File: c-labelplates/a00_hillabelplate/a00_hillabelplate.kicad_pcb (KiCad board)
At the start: 2 copper layers, 43 x 8 mm, 2 parts

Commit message: single gerbers
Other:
- board text added: "A00_hillabelplate"
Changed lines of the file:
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@@
       (outputformat 1)
       (mirror false)
-      (drillshape 1)
+      (drillshape 0)
       (scaleselection 1)
-      (outputdirectory "")
+      (outputdirectory "gerber/single/")
     )
   )
@@
   )
   (gr_circle (center 124.7 104) (end 124.78 104) (layer "F.SilkS") (width 0.15) (fill none))
+  (gr_line (start 110.4 100) (end 110.4 100.25) (layer "F.SilkS") (width 0.5))
   (gr_circle (center 130.75 101.3) (end 130.83 101.3) (layer "F.SilkS") (width 0.15) (fill none))
   (gr_circle (center 132.1 101.3) (end 132.18 101.3) (layer "F.SilkS") (width 0.15) (fill none))
   (gr_circle (center 128.4 104) (end 128.48 104) (layer "F.SilkS") (width 0.15) (fill none))
+  (gr_line (start 121.5 107.75) (end 121.5 108) (layer "F.SilkS") (width 0.5))
   (gr_circle (center 121 104) (end 121.08 104) (layer "F.SilkS") (width 0.15) (fill none))
   (gr_circle (center 125.7 101.3) (end 125.78 101.3) (layer "F.SilkS") (width 0.15) (fill none))
@@
   (gr_circle (center 113.6 106.7) (end 113.68 106.7) (layer "F.SilkS") (width 0.15) (fill none))
   (gr_circle (center 114.6 106.7) (end 114.68 106.7) (layer "F.SilkS") (width 0.15) (fill none))
+  (gr_line (start 125.2 107.75) (end 125.2 108) (layer "F.SilkS") (width 0.5))
+  (gr_line (start 128.9 100) (end 128.9 100.25) (layer "F.SilkS") (width 0.5))
   (gr_circle (center 118.3 104) (end 118.38 104) (layer "F.SilkS") (width 0.15) (fill none))
   (gr_circle (center 129.4 106.7) (end 129.48 106.7) (layer "F.SilkS") (width 0.15) (fill none))
@@
   (gr_circle (center 139.5 104) (end 139.58 104) (layer "F.SilkS") (width 0.15) (fill none))
   (gr_circle (center 132.1 104) (end 132.18 104) (layer "F.SilkS") (width 0.15) (fill none))
+  (gr_line (start 136.3 107.75) (end 136.3 108) (layer "F.SilkS") (width 0.5))
   (gr_circle (center 138.15 104) (end 138.23 104) (layer "F.SilkS") (width 0.15) (fill none))
   (gr_circle (center 132.1 106.7) (end 132.18 106.7) (layer "F.SilkS") (width 0.15) (fill none))
   (gr_circle (center 103.5 101.3) (end 103.58 101.3) (layer "F.SilkS") (width 0.15) (fill none))
+  (gr_line (start 117.8 100) (end 117.8 100.25) (layer "F.SilkS") (width 0.5))
   (gr_circle (center 134.45 106.7) (end 134.53 106.7) (layer "F.SilkS") (width 0.15) (fill none))
   (gr_circle (center 133.1 106.7) (end 133.18 106.7) (layer "F.SilkS") (width 0.15) (fill none))
@@
   (gr_circle (center 113.6 104) (end 113.68 104) (layer "F.SilkS") (width 0.15) (fill none))
   (gr_circle (center 136.8 106.7) (end 136.88 106.7) (layer "F.SilkS") (width 0.15) (fill none))
+  (gr_line (start 136.3 100) (end 136.3 100.25) (layer "F.SilkS") (width 0.5))
   (gr_circle (center 103.5 104) (end 103.58 104) (layer "F.SilkS") (width 0.15) (fill none))
   (gr_circle (center 119.65 106.7) (end 119.73 106.7) (layer "F.SilkS") (width 0.15) (fill none))
   (gr_circle (center 136.8 104) (end 136.88 104) (layer "F.SilkS") (width 0.15) (fill none))
   (gr_circle (center 136.8 101.3) (end 136.88 101.3) (layer "F.SilkS") (width 0.15) (fill none))
+  (gr_line (start 106.7 107.75) (end 106.7 108) (layer "F.SilkS") (width 0.5))
   (gr_circle (center 129.4 101.3) (end 129.48 101.3) (layer "F.SilkS") (width 0.15) (fill none))
   (gr_circle (center 124.7 101.3) (end 124.78 101.3) (layer "F.SilkS") (width 0.15) (fill none))
+  (gr_line (start 117.8 107.75) (end 117.8 108) (layer "F.SilkS") (width 0.5))
   (gr_circle (center 133.1 101.3) (end 133.18 101.3) (layer "F.SilkS") (width 0.15) (fill none))
   (gr_circle (center 134.45 101.3) (end 134.53 101.3) (layer "F.SilkS") (width 0.15) (fill none))
   (gr_circle (center 115.95 106.7) (end 116.03 106.7) (layer "F.SilkS") (width 0.15) (fill none))
+  (gr_line (start 132.6 100) (end 132.6 100.25) (layer "F.SilkS") (width 0.5))
   (gr_circle (center 106.2 104) (end 106.28 104) (layer "F.SilkS") (width 0.15) (fill none))
   (gr_circle (center 122 106.7) (end 122.08 106.7) (layer "F.SilkS") (width 0.15) (fill none))
@@
   (gr_circle (center 134.45 104) (end 134.53 104) (layer "F.SilkS") (width 0.15) (fill none))
   (gr_circle (center 124.7 106.7) (end 124.78 106.7) (layer "F.SilkS") (width 0.15) (fill none))
+  (gr_line (start 121.5 100) (end 121.5 100.25) (layer "F.SilkS") (width 0.5))
   (gr_circle (center 109.9 101.3) (end 109.98 101.3) (layer "F.SilkS") (width 0.15) (fill none))
   (gr_circle (center 122 104) (end 122.08 104) (layer "F.SilkS") (width 0.15) (fill none))
@@
   (gr_circle (center 138.15 101.3) (end 138.23 101.3) (layer "F.SilkS") (width 0.15) (fill none))
   (gr_circle (center 103.5 106.7) (end 103.58 106.7) (layer "F.SilkS") (width 0.15) (fill none))
+  (gr_line (start 128.9 107.75) (end 128.9 108) (layer "F.SilkS") (width 0.5))
   (gr_circle (center 123.35 106.7) (end 123.43 106.7) (layer "F.SilkS") (width 0.15) (fill none))
   (gr_circle (center 127.05 106.7) (end 127.13 106.7) (layer "F.SilkS") (width 0.15) (fill none))
   (gr_circle (center 114.6 101.3) (end 114.68 101.3) (layer "F.SilkS") (width 0.15) (fill none))
   (gr_line (start 100 100) (end 143 100) (layer "F.SilkS") (width 0.5))
+  (gr_line (start 125.2 100) (end 125.2 100.25) (layer "F.SilkS") (width 0.5))
   (gr_circle (center 104.85 104) (end 104.93 104) (layer "F.SilkS") (width 0.15) (fill none))
   (gr_line (start 100 108) (end 143 108) (layer "F.SilkS") (width 0.5))
@@
   (gr_circle (center 107.2 106.7) (end 107.28 106.7) (layer "F.SilkS") (width 0.15) (fill none))
   (gr_circle (center 112.25 106.7) (end 112.33 106.7) (layer "F.SilkS") (width 0.15) (fill none))
+  (gr_line (start 110.4 107.75) (end 110.4 108) (layer "F.SilkS") (width 0.5))
   (gr_circle (center 109.9 106.7) (end 109.98 106.7) (layer "F.SilkS") (width 0.15) (fill none))
   (gr_circle (center 113.6 101.3) (end 113.68 101.3) (layer "F.SilkS") (width 0.15) (fill none))
@@
   (gr_circle (center 127.05 104) (end 127.13 104) (layer "F.SilkS") (width 0.15) (fill none))
   (gr_circle (center 110.9 101.3) (end 110.98 101.3) (layer "F.SilkS") (width 0.15) (fill none))
+  (gr_line (start 114.1 100) (end 114.1 100.25) (layer "F.SilkS") (width 0.5))
   (gr_circle (center 117.3 104) (end 117.38 104) (layer "F.SilkS") (width 0.15) (fill none))
   (gr_circle (center 127.05 101.3) (end 127.13 101.3) (layer "F.SilkS") (width 0.15) (fill none))
   (gr_circle (center 139.5 101.3) (end 139.58 101.3) (layer "F.SilkS") (width 0.15) (fill none))
+  (gr_line (start 106.7 100) (end 106.7 100.25) (layer "F.SilkS") (width 0.5))
+  (gr_line (start 114.1 107.75) (end 114.1 108) (layer "F.SilkS") (width 0.5))
   (gr_circle (center 135.8 106.7) (end 135.88 106.7) (layer "F.SilkS") (width 0.15) (fill none))
   (gr_circle (center 115.95 101.3) (end 116.03 101.3) (layer "F.SilkS") (width 0.15) (fill none))
@@
   (gr_circle (center 135.8 101.3) (end 135.88 101.3) (layer "F.SilkS") (width 0.15) (fill none))
   (gr_circle (center 107.2 101.3) (end 107.28 101.3) (layer "F.SilkS") (width 0.15) (fill none))
+  (gr_line (start 132.6 107.75) (end 132.6 108) (layer "F.SilkS") (width 0.5))
   (gr_circle (center 119.65 104) (end 119.73 104) (layer "F.SilkS") (width 0.15) (fill none))
   (gr_line (start 136.3 100) (end 136.3 108) (layer "Cmts.User") (width 0.15))
@@
   (gr_line (start 100 108) (end 143 108) (layer "Edge.Cuts") (width 0.1))
   (gr_line (start 143 100) (end 143 108) (layer "Edge.Cuts") (width 0.1))
+  (gr_text "A00_hillabelplate" (at 133.35 106.299) (layer "B.SilkS")
+    (effects (font (size 1 1) (thickness 0.15)) (justify mirror))
+  )
 )

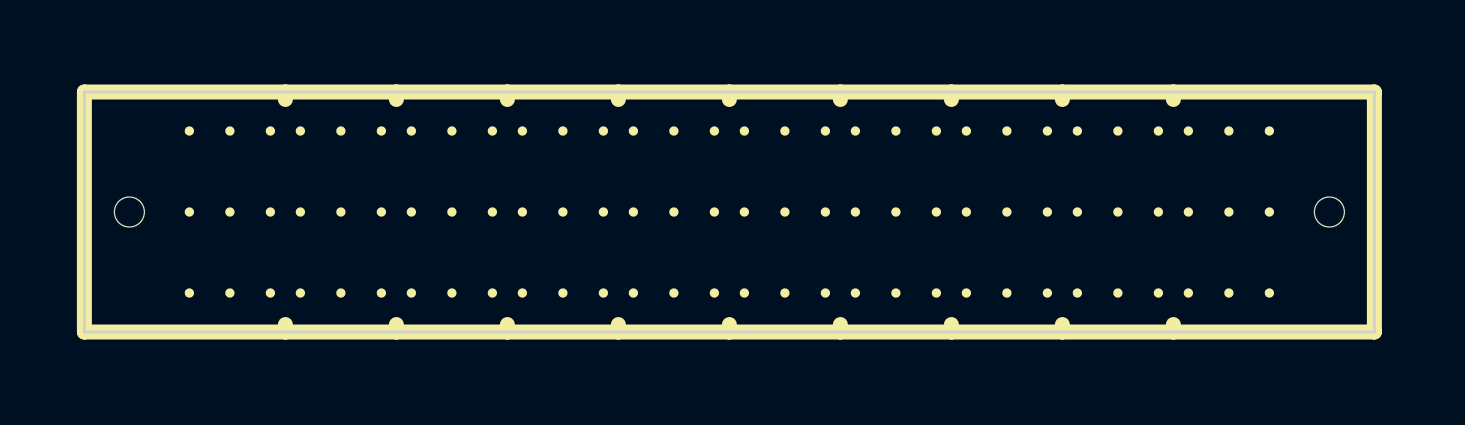
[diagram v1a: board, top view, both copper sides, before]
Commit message: added copper planes
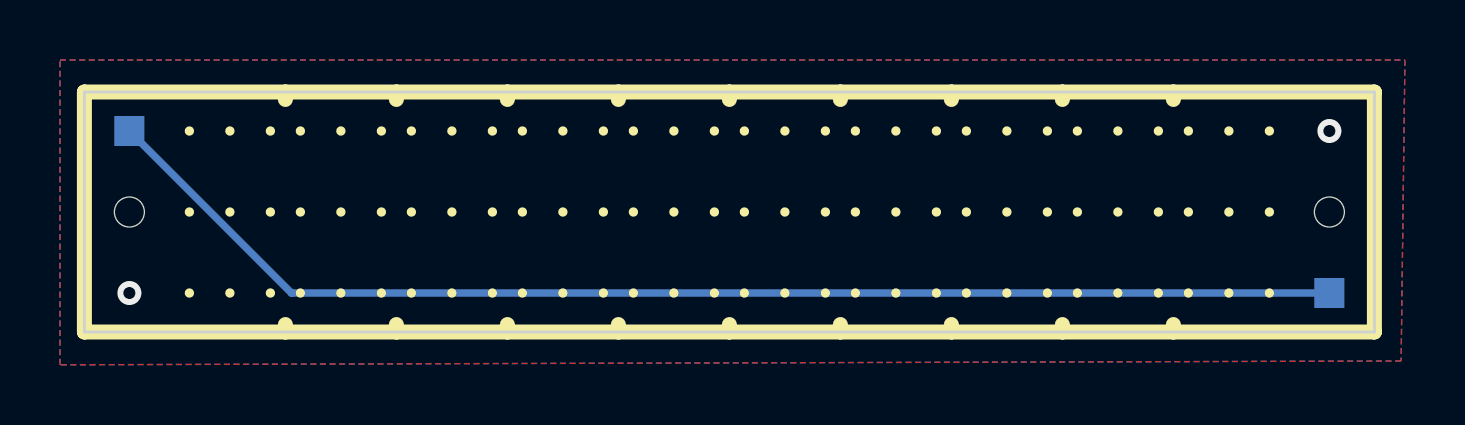
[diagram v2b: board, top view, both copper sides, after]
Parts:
- added TP1: TestPoint, TestPoint:TestPoint_Pad_1.0x1.0mm, B.Cu at (101.5, 101.3)
- added TP2: TestPoint, TestPoint:TestPoint_Pad_1.0x1.0mm, B.Cu at (141.5, 106.7)
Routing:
- net GND: track 0.00 -> 42.2 mm, vias 0 -> 2
- added copper zone on B.Cu, net GND
- added copper zone on F.Cu, net GND
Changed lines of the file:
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@@
   )
   (net 0 "")
+  (net 1 "GND")
   (footprint "MountingHoleSmall:MountingHole_1mm" (layer "F.Cu")
     (at 101.5 104)
@@
     (fp_circle (center 0 0) (end 1.25 0) (layer "F.CrtYd") (width 0.05) (fill none))
     (pad "" np_thru_hole circle locked (at 0 0) (size 1 1) (drill 1) (layers *.Cu *.Mask))
+  )
+  (footprint "TestPoint:TestPoint_Pad_1.0x1.0mm" (layer "B.Cu")
+    (at 141.5 106.7 180)
+    (descr "SMD rectangular pad as test Point, square 1.0mm side length")
+    (tags "test point SMD pad rectangle square")
+    (property "Sheetfile" "a00_hillabelplate.kicad_sch")
+    (property "Sheetname" "")
+    (attr exclude_from_pos_files)
+    (fp_text reference "TP2" (at 0 1.448) (layer "B.SilkS") hide
+      (effects (font (size 1 1) (thickness 0.15)) (justify mirror))
+    )
+    (fp_text value "TestPoint" (at 0 -1.55) (layer "B.Fab")
+      (effects (font (size 1 1) (thickness 0.15)) (justify mirror))
+    )
+    (fp_text user "${REFERENCE}" (at 0 1.45) (layer "B.Fab")
+      (effects (font (size 1 1) (thickness 0.15)) (justify mirror))
+    )
+    (fp_line (start -0.7 -0.7) (end -0.7 0.7) (layer "B.SilkS") (width 0.12))
+    (fp_line (start 0.7 0.7) (end 0.7 -0.7) (layer "B.SilkS") (width 0.12))
+    (fp_line (start 0.7 -0.7) (end -0.7 -0.7) (layer "B.SilkS") (width 0.12))
+    (fp_line (start -0.7 0.7) (end 0.7 0.7) (layer "B.SilkS") (width 0.12))
+    (fp_line (start -1 1) (end -1 -1) (layer "B.CrtYd") (width 0.05))
+    (fp_line (start -1 1) (end 1 1) (layer "B.CrtYd") (width 0.05))
+    (fp_line (start 1 -1) (end 1 1) (layer "B.CrtYd") (width 0.05))
+    (fp_line (start 1 -1) (end -1 -1) (layer "B.CrtYd") (width 0.05))
+    (pad "1" smd rect (at 0 0 180) (size 1 1) (layers "B.Cu" "B.Mask")
+      (net 1 "GND") (pinfunction "1") (pintype "passive"))
+  )
+  (footprint "TestPoint:TestPoint_Pad_1.0x1.0mm" (layer "B.Cu")
+    (at 101.5 101.3 180)
+    (descr "SMD rectangular pad as test Point, square 1.0mm side length")
+    (tags "test point SMD pad rectangle square")
+    (property "Sheetfile" "a00_hillabelplate.kicad_sch")
+    (property "Sheetname" "")
+    (attr exclude_from_pos_files)
+    (fp_text reference "TP1" (at -0.354 1.448) (layer "B.SilkS") hide
+      (effects (font (size 1 1) (thickness 0.15)) (justify mirror))
+    )
+    (fp_text value "TestPoint" (at 0 -1.55) (layer "B.Fab")
+      (effects (font (size 1 1) (thickness 0.15)) (justify mirror))
+    )
+    (fp_text user "${REFERENCE}" (at 0 1.45) (layer "B.Fab")
+      (effects (font (size 1 1) (thickness 0.15)) (justify mirror))
+    )
+    (fp_line (start -0.7 0.7) (end 0.7 0.7) (layer "B.SilkS") (width 0.12))
+    (fp_line (start 0.7 -0.7) (end -0.7 -0.7) (layer "B.SilkS") (width 0.12))
+    (fp_line (start 0.7 0.7) (end 0.7 -0.7) (layer "B.SilkS") (width 0.12))
+    (fp_line (start -0.7 -0.7) (end -0.7 0.7) (layer "B.SilkS") (width 0.12))
+    (fp_line (start -1 1) (end -1 -1) (layer "B.CrtYd") (width 0.05))
+    (fp_line (start -1 1) (end 1 1) (layer "B.CrtYd") (width 0.05))
+    (fp_line (start 1 -1) (end 1 1) (layer "B.CrtYd") (width 0.05))
+    (fp_line (start 1 -1) (end -1 -1) (layer "B.CrtYd") (width 0.05))
+    (pad "1" smd rect (at 0 0 180) (size 1 1) (layers "B.Cu" "B.Mask")
+      (net 1 "GND") (pinfunction "1") (pintype "passive"))
   )
   (gr_circle (center 124.7 104) (end 124.78 104) (layer "F.SilkS") (width 0.15) (fill none))
@@
   (gr_line (start 100 108) (end 143 108) (layer "Edge.Cuts") (width 0.1))
   (gr_line (start 143 100) (end 143 108) (layer "Edge.Cuts") (width 0.1))
-  (gr_text "A00_hillabelplate" (at 133.35 106.299) (layer "B.SilkS")
+  (gr_text "A00_hillabelplate" (at 133.477 106.807) (layer "B.SilkS")
     (effects (font (size 1 1) (thickness 0.15)) (justify mirror))
   )
+  (via (at 141.5 101.3) (size 0.8) (drill 0.4) (layers "F.Cu" "B.Cu") (free) (net 1))
+  (via (at 101.5 106.7) (size 0.8) (drill 0.4) (layers "F.Cu" "B.Cu") (free) (net 1))
+  (segment (start 141.5 106.7) (end 106.9 106.7) (width 0.25) (layer "B.Cu") (net 1))
+  (segment (start 106.9 106.7) (end 101.5 101.3) (width 0.25) (layer "B.Cu") (net 1))
+  (zone (net 1) (net_name "GND") (layers F&B.Cu) (hatch edge 0.508)
+    (connect_pads (clearance 0.508))
+    (min_thickness 0.254) (filled_areas_thickness no)
+    (fill yes (thermal_gap 0.508) (thermal_bridge_width 0.508))
+    (polygon
+      (pts
+        (xy 143.891 108.966)
+        (xy 99.187 109.093)
+        (xy 99.187 98.933)
+        (xy 144.018 98.933)
+      )
+    )
+  )
 )
